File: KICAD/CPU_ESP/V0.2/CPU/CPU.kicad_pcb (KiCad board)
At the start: 2 copper layers, 100 x 100 mm, 82 parts, among them J101 USB_B_Mini, J102 Conn_01x04, J501 Conn_02x20_Odd_Even, J502 Conn_02x20_Odd_Even, Q601 BSR19, Q602 BSR19, SW101 SW_Push_45deg, SW102 SW_Push_45deg, U201 LM75A, U202 PCA9306, U203 PCF8563T, U204 TCA9544A, U205 MCP23017_SS, U207 AT24CS01-SSHM, U301 LM1117DT-2.5, U401 ESP32-WROOM-32, U402 FT232RL, U403 TJA1051T, U601 SAA1064T, Y201 32.278kHz

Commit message: KICAD CMOS  CPU V0.2
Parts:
- J101: value USB_B_Mini -> USB_B_Micro; footprint Connector_USB:USB_Mini-B_Wuerth_65100516121_Horizontal -> Connector_USB:USB_Micro-B_Amphenol_10118194-0001LF_Horizontal
- moved D403 10.9 mm to (172.4, 149.0)
- moved R412 10.9 mm to (174.2, 144.0)
- moved R411 10.9 mm to (172.2, 144.0)
- moved C304 8.03 mm to (145.6, 84.8), turned to 0 degrees
- moved D401 6.46 mm to (133.1, 135.7)
- moved C406 6.46 mm to (135.7, 121.8)
- moved C408 6.46 mm to (136.2, 125.9)
- moved C407 6.46 mm to (152.5, 125.0)
- moved R402 6.46 mm to (135.4, 129.2)
- moved D402 6.46 mm to (133.1, 125.9)
- moved L401 6.46 mm to (136.5, 136.8)
- moved R404 6.46 mm to (152.9, 132.2)
- moved R405 6.46 mm to (152.9, 133.7)
- moved R406 6.46 mm to (152.9, 130.7)
- moved R407 6.46 mm to (152.9, 135.2)
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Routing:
- net +3.3V: track 383.1 -> 319.3 mm
- net +5VD: track 430.1 -> 396.5 mm, vias 18 -> 19
- net GND: track 673.6 -> 689.1 mm, vias 29 -> 11
- net Net-(U401-IO4): track 70.3 -> 55.3 mm
- net Net-(U401-IO2): track 66.3 -> 51.8 mm
- net /RESET: track 189.1 -> 178.2 mm, vias 6 -> 5
- net Net-(J601-Pin_3): track 32.3 -> 41.2 mm
- net /SDA-5V: track 166.3 -> 159.4 mm
- net /SCL-5V: track 156.5 -> 150.3 mm
- net /D0: track 86.5 -> 80.7 mm
- net /PWM4: track 32.6 -> 27.5 mm
- net /PWM0: track 33.8 -> 28.7 mm
- net /PWM2: track 32.6 -> 27.5 mm
- net /PWM3: track 35.6 -> 30.5 mm
- net /IO8: track 44.0 -> 38.9 mm
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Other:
- board size 100 x 100 mm -> 95.2 x 95.2 mm
- board text added: "V0.1 -> V 0.2 Correction taille PCB Correction position J501 et j502 Reprise du routage suite remise en place des composants USB MINI to MICRO"
- board text added: "V0.2 CMOS ESP32 NOV-2025"

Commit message: KICADUpdate
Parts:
- added C305: 10µ/10V, Capacitor_Tantalum_SMD:CP_EIA-3216-12_Kemet-S_HandSolder, F.Cu at (147.1, 80.3)
- C301: value 22µ -> 10µ/10V; footprint Capacitor_Tantalum_SMD:CP_EIA-3216-10_Kemet-I -> Capacitor_Tantalum_SMD:CP_EIA-3216-12_Kemet-S_HandSolder
- C304: value 22µ -> 10µ/10V; footprint Capacitor_Tantalum_SMD:CP_EIA-3528-21_Kemet-B -> Capacitor_Tantalum_SMD:CP_EIA-3216-12_Kemet-S_HandSolder
- C402: value 22µ/10V -> 10µ/10V
- C407: value 4.7µ/10V -> 10µ/10V
- D201: footprint Diode_SMD:D_1206_3216Metric -> Diode_SMD:D_2010_5025Metric_Pad1.52x2.65mm_HandSolder
- U201, U403: footprint Package_SO:SOIC-8_3.9x4.9mm_P1.27mm -> Package_SO:MSOP-8_3x3mm_P0.65mm
- moved D201 1.62 mm to (169.5, 112.7), turned to 0 degrees
- moved C301 0.45 mm to (147.2, 78.1)
- moved C304 0.24 mm to (145.4, 84.8)
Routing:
- net +5VD: track 396.5 -> 404.2 mm
- net Net-(D201-K): track 8.02 -> 7.12 mm
- net GND: track 689.1 -> 688.3 mm
- net /SDA-5V: track 159.4 -> 160.1 mm
- net /SCL-5V: track 150.3 -> 151.0 mm
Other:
- board text added: "V0.1 -> V 0.2 Correction taille PCB Correction position J501 et j502 Reprise du routage suite remise en place des composants USB MINI to MICRO C407 : 4.7µ => 10µ C402 ; 22µ => 10µ C304 ; 22µ => 10µ C301 ; 22µ => 10µ Add C305 : 10µ/10V D201 Changement Empreinte -> Diode_SMD:D_2010_5025Metric_Pad1.52x2.65mm_HandSolder U203 Changement Empreinte -> Package_SO:MSOP-8_3x3mm_P0.65mm"
- board text removed: "V0.1 -> V 0.2 Correction taille PCB Correction position J501 et j502 Reprise du routage suite remise en place des composants USB MINI to MICRO"

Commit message: KICAD MAJOR UPDATE V0.2
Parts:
- added Q401: BC817, Package_TO_SOT_SMD:SOT-23, F.Cu at (121.0, 139.6)
- added Q402: BC807, Package_TO_SOT_SMD:SOT-23, F.Cu at (121.0, 144.7)
- added R415: 10k, Resistor_SMD:R_0603_1608Metric, F.Cu at (115.4, 142.2)
- added R416: 10k, Resistor_SMD:R_0603_1608Metric, F.Cu at (115.4, 139.8)
- C203: value 10n -> 10p
- R405: value NC -> 0
- R408, R409: value 4k7 -> 330
- U403: footprint Package_SO:MSOP-8_3x3mm_P0.65mm -> Package_SO:SOIC-8_3.9x4.9mm_P1.27mm
- moved R407 42.8 mm to (110.7, 142.9)
- moved C304 42.8 mm to (103.2, 92.4)
- moved C305 42.8 mm to (105.0, 87.9)
- moved D401 42.8 mm to (91.0, 143.4)
- moved D402 42.8 mm to (91.0, 133.5)
- moved R408 42.8 mm to (91.0, 140.1)
- moved R409 42.8 mm to (91.0, 136.7)
- moved C408 42.8 mm to (94.0, 133.5)
- moved C303 42.8 mm to (101.7, 81.5)
- moved C402 42.8 mm to (116.2, 86.6)
- moved C406 42.8 mm to (93.5, 129.4)
- moved D201 42.8 mm to (127.3, 120.3)
- moved D301 42.8 mm to (111.0, 86.6)
- moved J102 42.8 mm to (139.9, 154.0)
- moved J502 42.8 mm to (175.3, 69.6)
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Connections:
- R404 pad 2: /RESET -> /ESP32 Module/RTS
- R405 pad 2: unconnected-(R405-Pad2) -> /ESP32 Module/DTR
- R413 pad 2: Net-(U401-IO35) -> Net-(U401-IO5)
- U401 pad 29: /T2CK -> Net-(U401-IO5)
- U401 pad 7: Net-(U401-IO35) -> /T2CK
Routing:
- net Net-(U401-IO5): track 0.00 -> 76.9 mm, vias 0 -> 4
- net Net-(U401-IO35): track 63.5 -> 0.00 mm, vias 2 -> 0
- net /ESP32 Module/BOOT: track 19.2 -> 72.8 mm, vias 2 -> 5
- net /RW: track 72.3 -> 102.3 mm
- net /T2CK: track 47.4 -> 74.7 mm
- net Net-(C201-Pad1): track 4.29 -> 23.7 mm, vias 0 -> 2
- net /ESP32 Module/RTS: track 0.00 -> 19.4 mm, vias 0 -> 2
- net GND: track 688.3 -> 671.0 mm, vias 11 -> 21
- net /ESP32 Module/DTR: track 0.00 -> 12.0 mm
- net Net-(Q402-B): track 0.00 -> 8.29 mm, vias 0 -> 2
- net +5VD: track 404.2 -> 410.6 mm
- net /RESET: track 178.2 -> 171.9 mm, vias 5 -> 6
- net Net-(Q401-B): track 0.00 -> 5.24 mm
- net /SDA1: track 36.8 -> 32.8 mm
- net /SDA-5V: track 160.1 -> 162.6 mm
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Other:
- board text added: "+12V"
- board text added: "+3.3V"
- board text added: "+5VA"
- board text added: "+5VD"
- board text added: "+BATT"
- board text added: "D1"
- board text added: "D3"
- board text added: "D5"
- board text added: "D7"
- board text added: "GND"
- board text added: "IO0"
- board text added: "IO1"
- board text added: "IO2"
- board text added: "IO3"
- board text added: "IO4"
- board text added: "IO5"
- board text added: "IO6"
- board text added: "IO7"
- board text added: "IO8"
- board text added: "PWM0"
- board text added: "PWM1"
- board text added: "PWM2"
- board text added: "PWM3"
- board text added: "PWM4"
- board text added: "RESET"
- board text added: "RETRO"
- board text added: "RS"
- board text added: "RX1"
- board text added: "RX2"
- board text added: "SCS"
- board text added: "SDA0"
- board text added: "SDA1"
- board text added: "SDA2"
- board text added: "T1CK"
- board text added: "V0.1 -> V 0.2 Correction taille PCB Correction position J501 et j502 Reprise du routage suite remise en place des composants USB MINI to MICRO C407 : 4.7µ => 10µ C402 ; 22µ => 10µ C304 ; 22µ => 10µ C301 ; 22µ => 10µ Add C305 : 10µ/10V D201 Changement Empreinte -> Diode_SMD:D_2010_5025Metric_Pad1.52x2.65mm_HandSolder U203 Changement Empreinte -> Package_SO:MSOP-8_3x3mm_P0.65mm R408 et R409 => chan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"
- board text removed: "V0.1 -> V 0.2 Correction taille PCB Correction position J501 et j502 Reprise du routage suite remise en place des composants USB MINI to MICRO C407 : 4.7µ => 10µ C402 ; 22µ => 10µ C304 ; 22µ => 10µ C301 ; 22µ => 10µ Add C305 : 10µ/10V D201 Changement Empreinte -> Diode_SMD:D_2010_5025Metric_Pad1.52x2.65mm_HandSolder U203 Changement Empreinte -> Package_SO:MSOP-8_3x3mm_P0.65mm"

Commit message: VSCODE update
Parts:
- added J103: Conn_01x04, Connector_JST:JST_GH_SM04B-GHS-TB_1x04-1MP_P1.25mm_Horizontal, F.Cu at (104.7, 153.7)
- moved J101 6.91 mm to (94.3, 152.4)
- moved L401 0.35 mm to (94.0, 144.5), turned to 90 degrees
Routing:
- net /RX1: track 36.2 -> 115.9 mm, vias 2 -> 4
- net /TX1: track 32.8 -> 112.1 mm, vias 0 -> 2
- net +5VD: track 410.6 -> 488.9 mm, vias 19 -> 20
- net /RW: track 102.3 -> 93.5 mm
- net GND: track 671.0 -> 664.2 mm
- net /ESP32 Module/D+: track 20.6 -> 25.9 mm
- net /ESP32 Module/D-: track 19.0 -> 23.8 mm
- net /ESP32 Module/VCCUSB: track 9.90 -> 5.84 mm
- net /SCL1: track 43.0 -> 39.0 mm
- net /SCK: track 63.7 -> 67.3 mm
- net /SCS: track 65.2 -> 68.6 mm
- net /RESET: track 171.9 -> 174.2 mm, vias 6 -> 7
- net /RS: track 49.3 -> 50.8 mm
- net /ESP32 Module/CAN-RX: track 48.3 -> 49.5 mm
- net /E: track 61.7 -> 62.9 mm
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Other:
- board text added: "I2C"
- board text added: "UART COMMAND"
- board text added: "UART DEBUG"

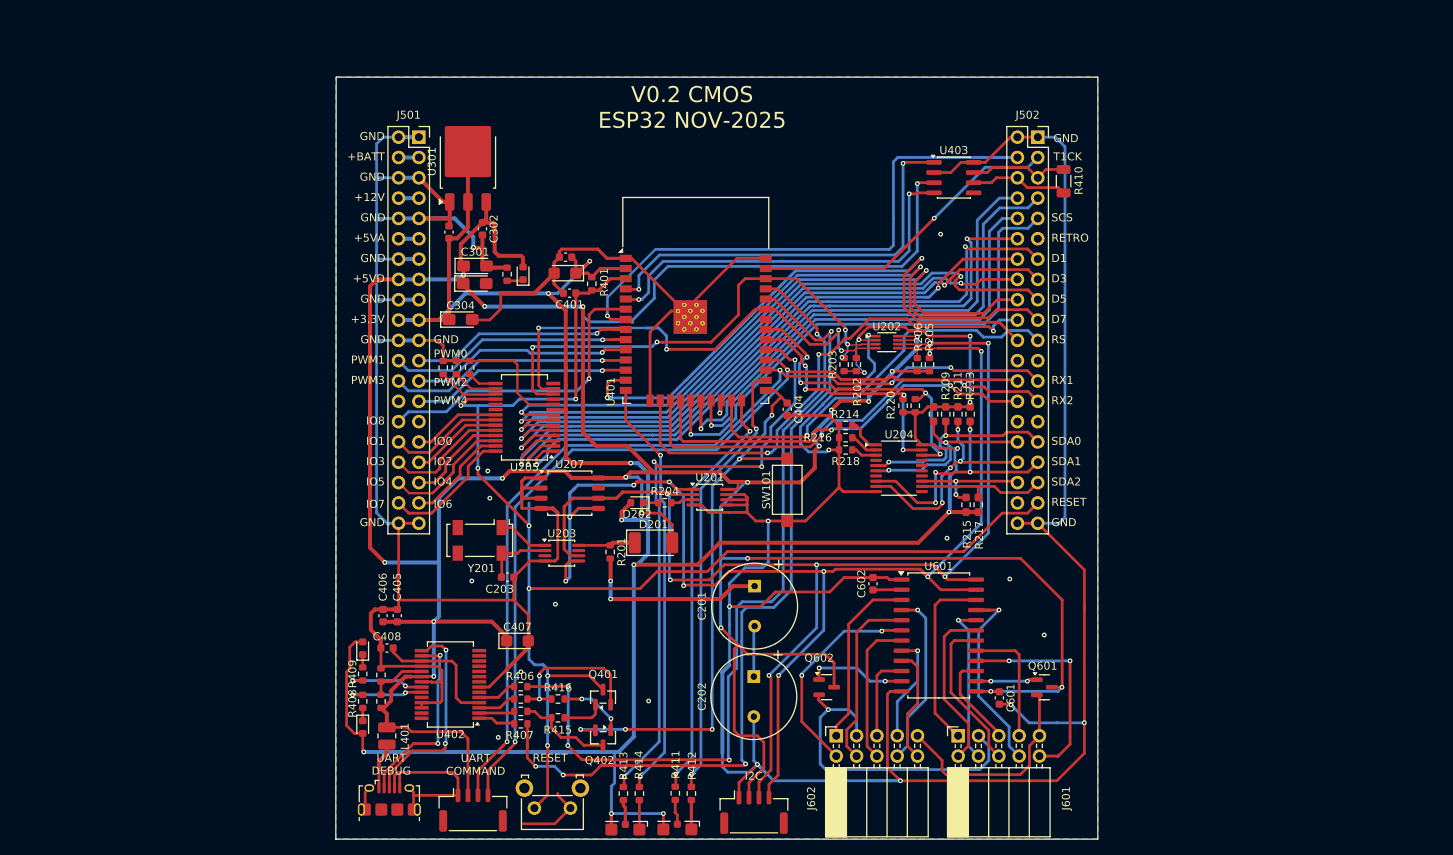
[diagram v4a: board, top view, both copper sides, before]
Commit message: KICAD 4 UART update
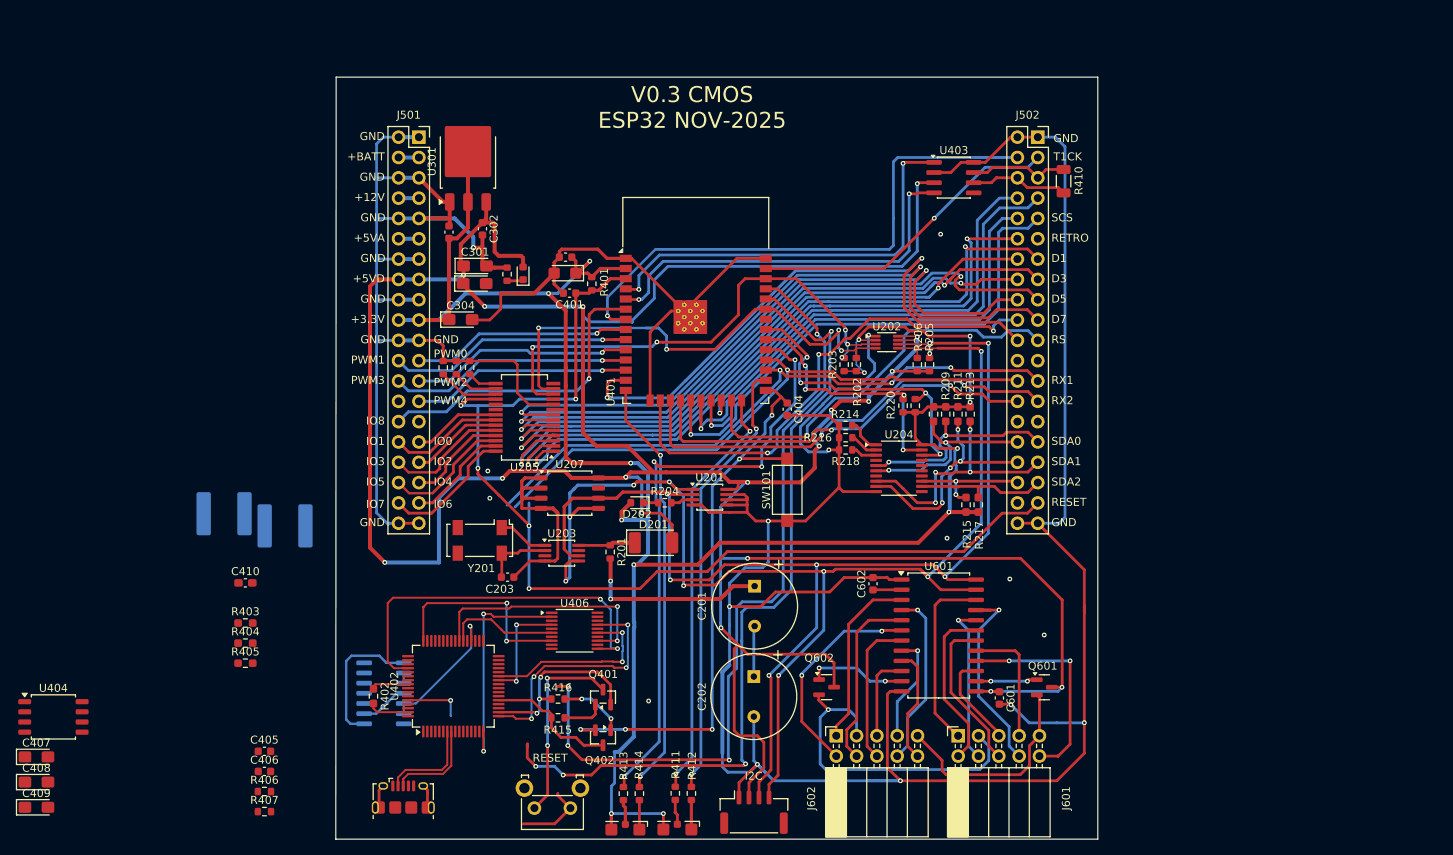
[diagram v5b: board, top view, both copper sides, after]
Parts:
- removed D401, D402: ORANGE, LED_SMD:LED_0603_1608Metric
- removed J103: Conn_01x04, Connector_JST:JST_GH_SM04B-GHS-TB_1x04-1MP_P1.25mm_Horizontal
- removed R408, R409: 330, Resistor_SMD:R_0603_1608Metric
- added C409: 10µ/10V, Capacitor_Tantalum_SMD:CP_EIA-3216-12_Kemet-S_HandSolder, F.Cu at (50.2, 153.4)
- added C410: 100n, Capacitor_SMD:C_0603_1608Metric_Pad1.08x0.95mm_HandSolder, F.Cu at (76.3, 125.3)
- added L402: 39µH, Capacitor_SMD:C_2220_5750Metric, B.Cu at (81.3, 118.2)
- added U404: 93C46, Package_SO:SOIC-8_5.3x5.3mm_P1.27mm, F.Cu at (52.3, 142.1)
- added U405: 74HC02, Package_SO:SOIC-14_3.9x8.7mm_P1.27mm, B.Cu at (93.6, 139.1)
- added U406: 74HC244, Package_SO:TSSOP-20_4.4x5mm_P0.5mm, F.Cu at (117.4, 131.3)
- C405, C406: value 100n -> 27P
- C407: footprint Capacitor_Tantalum_SMD:CP_EIA-3216-12_Kemet-S -> Capacitor_Tantalum_SMD:CP_EIA-3216-12_Kemet-S_HandSolder
- C408: value 100n -> 10µ/10V; footprint Capacitor_SMD:C_0603_1608Metric -> Capacitor_Tantalum_SMD:CP_EIA-3216-12_Kemet-S_HandSolder
- L401: value 22µ -> 39µH; footprint Inductor_SMD:L_1008_2520Metric -> Capacitor_SMD:C_2220_5750Metric; moved to B.Cu
- R402, R403: value 2k2 -> 10k; footprint Resistor_SMD:R_0603_1608Metric -> Resistor_SMD:R_0603_1608Metric_Pad0.98x0.95mm_HandSolder
- R404: value 0 -> 10k; footprint Resistor_SMD:R_0603_1608Metric -> Resistor_SMD:R_0603_1608Metric_Pad0.98x0.95mm_HandSolder
- R405: value 0 -> 2K2; footprint Resistor_SMD:R_0603_1608Metric -> Resistor_SMD:R_0603_1608Metric_Pad0.98x0.95mm_HandSolder
- R406: value 0 -> 1k
- R407: value 0 -> 12k
- U402: value FT232RL -> FT4232H; footprint Package_SO:SSOP-28_5.3x10.2mm_P0.65mm -> Package_QFP:TQFP-64_10x10mm_P0.5mm
- moved C407 61.9 mm to (50.2, 147.1)
- moved C408 46.9 mm to (50.2, 150.2)
- moved R404 35.1 mm to (76.3, 132.9)
- moved R405 35.0 mm to (76.3, 135.4)
- moved R406 34.6 mm to (78.7, 151.4)
- moved L401 34.4 mm to (73.6, 116.7), turned to 180 degrees
- moved R407 33.9 mm to (78.7, 153.9)
- moved C406 24.5 mm to (78.7, 148.9), turned to 0 degrees
- moved C405 23.7 mm to (78.7, 146.4), turned to 0 degrees
- moved R403 19.6 mm to (76.3, 130.4), turned to 0 degrees
- moved R402 2.82 mm to (92.3, 139.5), turned to -90 degrees
- moved J101 1.76 mm to (96.0, 152.1)
- moved U402 0.42 mm to (102.3, 138.3), turned to 90 degrees
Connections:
- C405 pad 1: +5VD -> Net-(U402-OSCI)
- C406 pad 1: +5VD -> Net-(U402-OSCO)
- C407 pad 1: +5VD -> Net-(U402-VREGOUT)
- C408 pad 1: GND -> Net-(U402-VPHY)
- C408 pad 2: Net-(U402-3V3OUT) -> GND
- J101 pad 1: /ESP32 Module/VCCUSB -> /VCCUSB
- L401 pad 1: /ESP32 Module/VCCUSB -> +3.3V
- L401 pad 2: +5VD -> Net-(U402-VPHY)
- R402 pad 1: Net-(U402-~{RESET}) -> +3.3V
- R402 pad 2: GND -> Net-(U402-EECS)
- R403 pad 1: +5VD -> +3.3V
- R403 pad 2: Net-(U402-~{RESET}) -> Net-(U404-DO)
- R404 pad 1: Net-(U402-RTS) -> +3.3V
- R404 pad 2: /ESP32 Module/RTS -> Net-(U402-EECLK)
- R405 pad 1: Net-(U402-DTR) -> Net-(U404-DO)
- R405 pad 2: /ESP32 Module/DTR -> Net-(U402-EEDATA)
- R406 pad 1: Net-(U402-RXD) -> +3.3V
- R406 pad 2: /TX0 -> Net-(U402-~{RESET})
- R407 pad 1: Net-(U402-TXD) -> GND
- R407 pad 2: /RX0 -> Net-(U402-REF)
- U402 pad 1: Net-(U402-TXD) -> GND
- U402 pad 10: unconnected-(U402-DCD-Pad10) -> GND
- U402 pad 11: unconnected-(U402-CTS-Pad11) -> GND
- U402 pad 12: unconnected-(U402-CBUS4-Pad12) -> Net-(U402-VREGOUT)
- U402 pad 13: unconnected-(U402-CBUS2-Pad13) -> GND
- U402 pad 14: unconnected-(U402-CBUS3-Pad14) -> Net-(U402-~{RESET})
- U402 pad 15: /ESP32 Module/D+ -> GND
- U402 pad 16: /ESP32 Module/D- -> /ESP32 Module/TX0A
- U402 pad 17: Net-(U402-3V3OUT) -> /ESP32 Module/RX0A
- U402 pad 18: GND -> /ESP32 Module/RTS
- U402 pad 19: Net-(U402-~{RESET}) -> /ESP32 Module/CTS
- U402 pad 2: Net-(U402-DTR) -> Net-(U402-OSCI)
- U402 pad 20: +5VD -> +3.3V
- U402 pad 21: GND -> /ESP32 Module/DTR
- U402 pad 22: Net-(U402-CBUS1) -> /ESP32 Module/DSR
- U402 pad 23: Net-(U402-CBUS0) -> /ESP32 Module/DCD
- U402 pad 24: (no net) -> /ESP32 Module/RING
- U402 pad 26: GND -> /ESP32 Module/TX1A
- U402 pad 27: unconnected-(U402-OSCI-Pad27) -> /ESP32 Module/RX1A
- U402 pad 3: Net-(U402-RTS) -> Net-(U402-OSCO)
- U402 pad 4: Net-(U402-3V3OUT) -> Net-(U402-VPHY)
- U402 pad 5: Net-(U402-RXD) -> GND
- U402 pad 6: unconnected-(U402-RI-Pad6) -> Net-(U402-REF)
- U402 pad 7: GND -> /ESP32 Module/D-
- U402 pad 8: (no net) -> /ESP32 Module/D+
- U402 pad 9: unconnected-(U402-DCR-Pad9) -> Net-(U402-VPLL)
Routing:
- net GND: track 664.2 -> 569.9 mm, vias 21 -> 17
- net +5VD: track 488.9 -> 427.3 mm, vias 20 -> 18
- net /ESP32 Module/RX3A: track 0.00 -> 47.2 mm, vias 0 -> 2
- net +3.3V: track 318.9 -> 275.7 mm, vias 14 -> 13
- net /RX1: track 115.9 -> 78.1 mm, vias 4 -> 3
- net /TX1: track 112.1 -> 74.6 mm, vias 2 -> 1
- net /ESP32 Module/RX0A: track 0.00 -> 31.0 mm, vias 0 -> 4
- net /ESP32 Module/RX2A: track 0.00 -> 30.5 mm, vias 0 -> 2
- net /ESP32 Module/TX0A: track 0.00 -> 28.3 mm, vias 0 -> 2
- net /ESP32 Module/TX3A: track 0.00 -> 25.3 mm, vias 0 -> 2
- net /ESP32 Module/RX1A: track 0.00 -> 23.1 mm, vias 0 -> 2
- net Net-(U405-Pad1): track 0.00 -> 17.6 mm
- net Net-(U402-~{SUSPEND}): track 0.00 -> 17.3 mm, vias 0 -> 1
- net Net-(U402-3V3OUT): track 16.3 -> 0.00 mm
- net /ESP32 Module/TX2A: track 0.00 -> 14.2 mm
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- removed copper zone on B.Cu, net GND
- removed copper zone on F.Cu, net GND
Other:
- board text added: "V0.3 CMOS ESP32 NOV-2025"
- board text removed: "UART COMMAND"
- board text removed: "UART DEBUG"
- board text removed: "V0.2 CMOS ESP32 NOV-2025"
